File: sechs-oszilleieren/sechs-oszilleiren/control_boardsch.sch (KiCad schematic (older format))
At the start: 22 parts

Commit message: Added board connector pins and reformatted the schematic to account for 2 board design.
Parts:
- added D? (x4): R, LED_THT:LED_D3.0mm, symbol Device:LED_Small_ALT
- added J?: Conn_01x02_Male, symbol Connector:Conn_01x02_Male
- added J? (x12): AudioJack2, Connector_Audio:Jack_3.5mm_QingPu_WQP-PJ398SM_Vertical_CircularHoles, symbol Connector:AudioJack2
- added J?: Conn_01x05_Male, symbol Connector:Conn_01x05_Male
- added J?: Conn_01x09_Male, symbol Connector:Conn_01x09_Male
- added J?: Conn_01x12_Male, symbol Connector:Conn_01x12_Male
- added J?: Conn_01x06_Male, symbol Connector:Conn_01x06_Male
- added Q? (x4): 2N3904, Package_TO_SOT_SMD:SOT-23, symbol Transistor_BJT:2N3904
- added R? (x4): 2K, Resistor_SMD:R_0805_2012Metric, symbol Device:R_Small_US
- added R? (x4): 47K, Resistor_SMD:R_0805_2012Metric, symbol Device:R_Small_US
- added RV? (x4): B100K, Potentiometer_THT:Potentiometer_Alpha_RD901F-40-00D_Single_Vertical_CircularHoles, symbol Device:R_POT_US
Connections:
- net labels added: level_pot_1, level_pot_w, out_1, out_2, output_1, output_2, output_indicator, vco_a_cv, vco_a_pitch_3, vco_b_cv, vco_b_out, vco_b_pitch_1, vco_b_pitch_2, vco_b_pitch_3, vco_c_cv, vco_c_out, vco_c_pitch_1, vco_c_pitch_2, vco_c_pitch_3, vco_d_cv, vco_d_out, vco_d_pitch_1, vco_d_pitch_2, vco_d_pitch_3, vco_d_sync, vco_e_cv, vco_e_out, vco_e_pitch_1, vco_e_pitch_2, vco_e_pitch_3, vco_e_sync, vco_f_cv, vco_f_pitch_3, vco_f_sync
- net labels removed: mix_feedback, vco_sync_d
- wire segments 59 -> 258
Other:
- moved on the sheet: D?, J?, Q?, R?, RV?

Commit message: Added pins between boards for stacking. Changed all components to THT components.
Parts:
- J16: renamed from J?; footprint (none) -> Connector_PinHeader_2.54mm:PinHeader_1x02_P2.54mm_Vertical
- J19: renamed from J?; footprint (none) -> Connector_PinHeader_2.54mm:PinHeader_1x09_P2.54mm_Vertical
- J20: renamed from J?; footprint (none) -> Connector_PinHeader_2.54mm:PinHeader_1x12_P2.54mm_Vertical
- J21: renamed from J?; footprint (none) -> Connector_PinHeader_2.54mm:PinHeader_1x06_P2.54mm_Vertical
- J22: renamed from J?; footprint (none) -> Connector_PinHeader_2.54mm:PinHeader_1x05_P2.54mm_Vertical
- Q1, Q2, Q3, Q4, Q5, Q6, Q7: renamed from Q?; footprint Package_TO_SOT_SMD:SOT-23 -> Package_TO_SOT_THT:TO-92
- R1, R10, R11, R12, R13, R14, R15, R2, R3, R4, R5, R6, R7, R8, R9: renamed from R?; footprint Resistor_SMD:R_0805_2012Metric -> Resistor_THT:R_Axial_DIN0204_L3.6mm_D1.6mm_P7.62mm_Horizontal
- gave numbers to parts that had none: 32

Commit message: Added a number of stages for the attenuverter, vco, and sechs_oszilleieren.
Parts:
- removed D1, D2, D3, D4, D5, D6, D7: R, LED_THT:LED_D3.0mm, symbol Device:LED_Small_ALT
- removed D8: Y, LED_THT:LED_D3.0mm, symbol Device:LED_Small_ALT
- removed J1, J10, J11, J12, J13, J14, J15, J17, J18, J2, J3, J4, J5, J6, J7, J8, J9: AudioJack2, Connector_Audio:Jack_3.5mm_QingPu_WQP-PJ398SM_Vertical_CircularHoles, symbol Connector:AudioJack2
- removed J16: Conn_01x02_Male, Connector_PinHeader_2.54mm:PinHeader_1x02_P2.54mm_Vertical, symbol Connector:Conn_01x02_Male
- removed J19: Conn_01x09_Male, Connector_PinHeader_2.54mm:PinHeader_1x09_P2.54mm_Vertical, symbol Connector:Conn_01x09_Male
- removed J20: Conn_01x12_Male, Connector_PinHeader_2.54mm:PinHeader_1x12_P2.54mm_Vertical, symbol Connector:Conn_01x12_Male
- removed J21: Conn_01x06_Male, Connector_PinHeader_2.54mm:PinHeader_1x06_P2.54mm_Vertical, symbol Connector:Conn_01x06_Male
- removed J22: Conn_01x05_Male, Connector_PinHeader_2.54mm:PinHeader_1x05_P2.54mm_Vertical, symbol Connector:Conn_01x05_Male
- removed Q1, Q2, Q3, Q4, Q5, Q6, Q7: 2N3904, Package_TO_SOT_THT:TO-92, symbol Transistor_BJT:2N3904
- removed R1, R14, R2, R3, R7, R8, R9: 47K, Resistor_THT:R_Axial_DIN0204_L3.6mm_D1.6mm_P7.62mm_Horizontal, symbol Device:R_Small_US
- removed R10, R11, R12, R15, R4, R5, R6: 2K, Resistor_THT:R_Axial_DIN0204_L3.6mm_D1.6mm_P7.62mm_Horizontal, symbol Device:R_Small_US
- removed R13: 22K, Resistor_THT:R_Axial_DIN0204_L3.6mm_D1.6mm_P7.62mm_Horizontal, symbol Device:R_Small_US
- removed RV1, RV2, RV3, RV4, RV5, RV6: B100K, Potentiometer_THT:Potentiometer_Alpha_RD901F-40-00D_Single_Vertical_CircularHoles, symbol Device:R_POT_US
- removed RV7: A10K, Potentiometer_THT:Potentiometer_Alpha_RD901F-40-00D_Single_Vertical_CircularHoles, symbol Device:R_POT_US
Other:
- note removed: "LEVEL"
- note removed: "LFO Stage"
- note removed: "Mixer Controls"
- note removed: "Power Indicators"
- note removed: "VCO Stage"

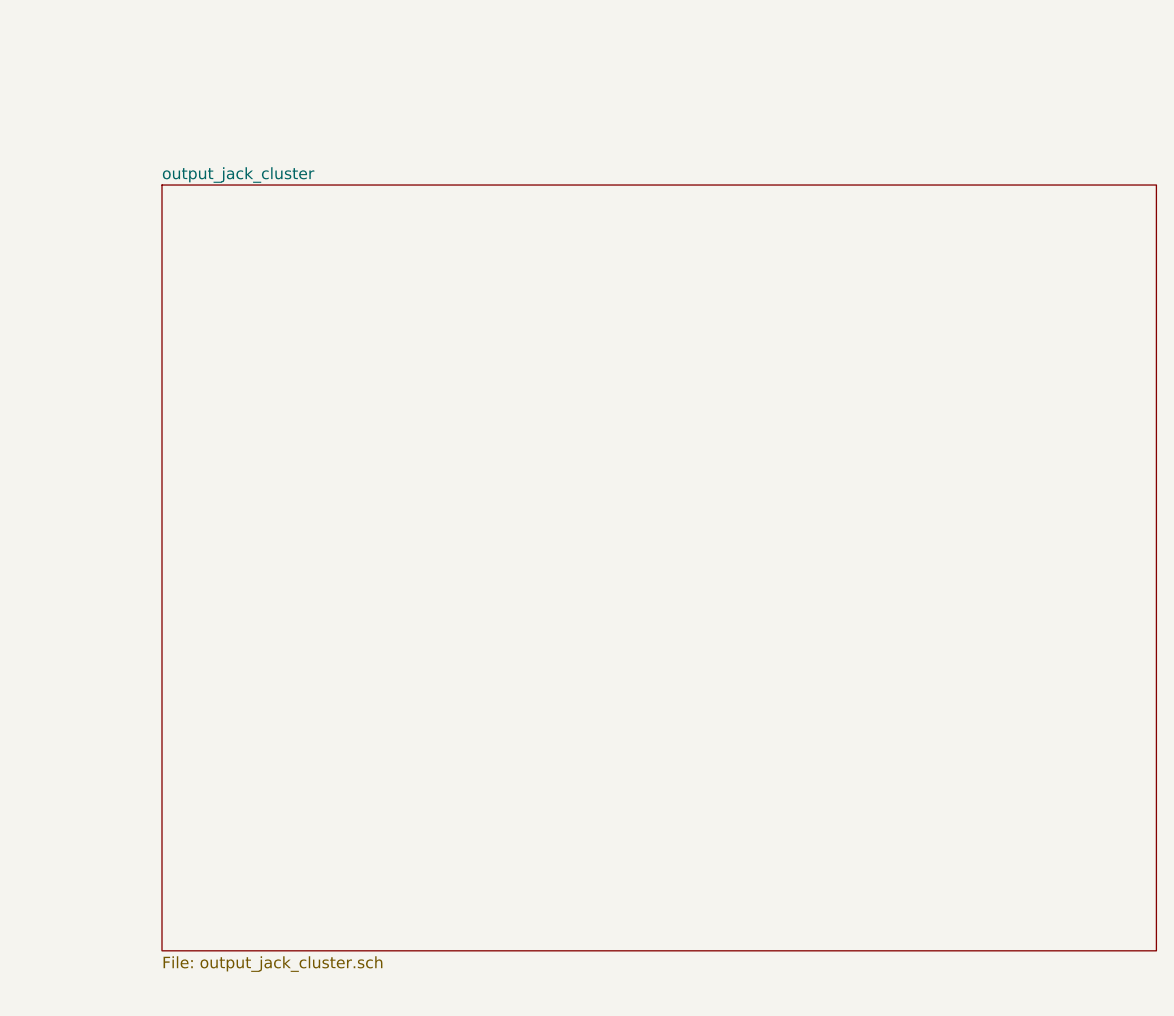
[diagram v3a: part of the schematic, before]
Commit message: Rearranged labeling on voice board, simplified output stage and reduced part count. Simplified CD40106 feedback nets.
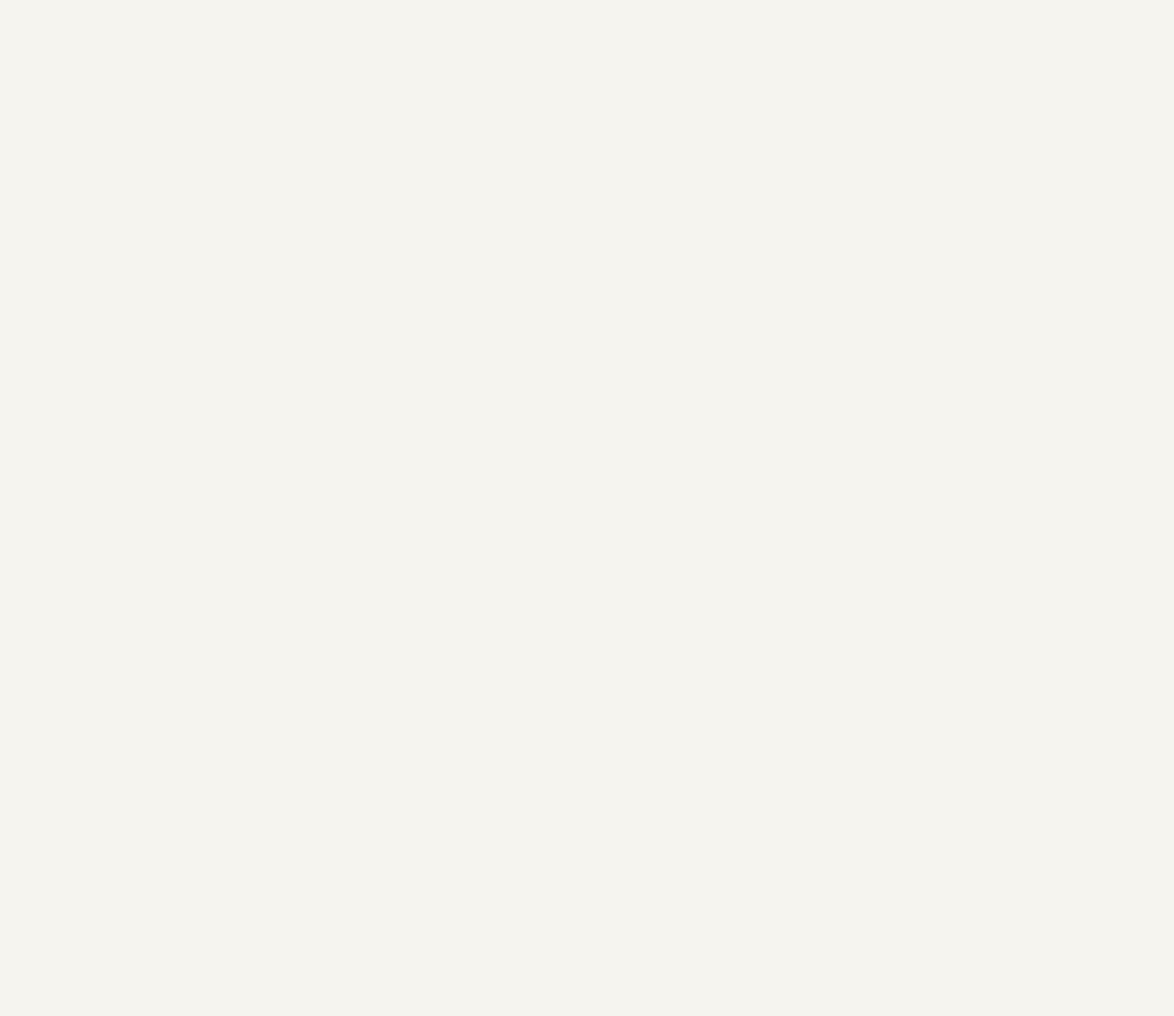
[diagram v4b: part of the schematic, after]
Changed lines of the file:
@@
 $Descr B 17000 11000
 encoding utf-8
-Sheet 2 12
+Sheet 2 11
 Title "Sechs-Oszilléierer"
 Date "2020-04-04"
@@
 F1 "output_control_clustersch.sch" 50
 $EndSheet
-$Sheet
-S 10400 4900 4350 3350
-U 5E8AD7DE
-F0 "output_jack_cluster" 50
-F1 "output_jack_cluster.sch" 50
-$EndSheet
 $EndSCHEMATC
